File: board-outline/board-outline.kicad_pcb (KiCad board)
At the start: 2 copper layers, 162 x 136.8 mm, 1 part

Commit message: all done :)
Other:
- board size 162 x 136.8 mm -> 160 x 136.8 mm
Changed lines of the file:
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@@
 	)
 	(footprint "691378140024-2:J_Wurth_WR-TBL_691378140024"
+		(locked yes)
 		(layer "F.Cu")
 		(at 234.25 110.14 180)
@@
 			)
 		)
-		(attr through_hole)
+		(attr through_hole dnp)
 		(duplicate_pad_numbers_are_jumpers no)
 		(fp_line
@@
 		(layer "F.SilkS")
 	)
+	(gr_line
+		(start 190.39 80)
+		(end 194 80)
+		(stroke
+			(width 0.1)
+			(type default)
+		)
+		(locked yes)
+		(layer "F.SilkS")
+	)
+	(gr_line
+		(start 190.39 99.53)
+		(end 190.39 80)
+		(stroke
+			(width 0.1)
+			(type default)
+		)
+		(locked yes)
+		(layer "F.SilkS")
+	)
+	(gr_line
+		(start 239.61 80)
+		(end 236 80)
+		(stroke
+			(width 0.1)
+			(type default)
+		)
+		(locked yes)
+		(layer "F.SilkS")
+	)
+	(gr_line
+		(start 239.61 99.53)
+		(end 239.61 80)
+		(stroke
+			(width 0.1)
+			(type default)
+		)
+		(locked yes)
+		(layer "F.SilkS")
+	)
 	(gr_poly
 		(pts
@@
 	(gr_line
 		(start 135 93.5)
-		(end 135 165.5)
-		(stroke
-			(width 0.05)
-			(type default)
-		)
-		(layer "Edge.Cuts")
-	)
-	(gr_line
-		(start 155 93.5)
+		(end 155 93.5)
+		(stroke
+			(width 0.05)
+			(type solid)
+		)
+		(locked yes)
+		(layer "Edge.Cuts")
+	)
+	(gr_line
+		(start 135 165.5)
 		(end 135 93.5)
 		(stroke
 			(width 0.05)
-			(type default)
-		)
+			(type solid)
+		)
+		(locked yes)
 		(layer "Edge.Cuts")
 	)
@@
 		(stroke
 			(width 0.05)
-			(type default)
-		)
+			(type solid)
+		)
+		(locked yes)
 		(layer "Edge.Cuts")
 	)
@@
 		(stroke
 			(width 0.05)
-			(type default)
-		)
+			(type solid)
+		)
+		(locked yes)
 		(layer "Edge.Cuts")
 	)
@@
 			(type default)
 		)
+		(locked yes)
 		(layer "Edge.Cuts")
 	)
@@
 			(type default)
 		)
+		(locked yes)
 		(layer "Edge.Cuts")
 	)
@@
 		(stroke
 			(width 0.05)
-			(type default)
-		)
+			(type solid)
+		)
+		(locked yes)
 		(layer "Edge.Cuts")
 	)
@@
 			(type default)
 		)
+		(locked yes)
 		(layer "Edge.Cuts")
 	)
 	(gr_rect
 		(start 275 93.5)
-		(end 297 165.5)
-		(stroke
-			(width 0.05)
-			(type default)
+		(end 295 165.5)
+		(stroke
+			(width 0.05)
+			(type solid)
 		)
 		(fill no)
+		(locked yes)
 		(layer "Edge.Cuts")
 	)
@@
 			)
 		)
+	)
+	(zone
+		(locked yes)
+		(layer "F.SilkS")
+		(hatch edge 0.5)
+		(connect_pads
+			(clearance 0)
+		)
+		(min_thickness 0.25)
+		(keepout
+			(tracks not_allowed)
+			(vias not_allowed)
+			(pads not_allowed)
+			(copperpour allowed)
+			(footprints not_allowed)
+		)
+		(placement
+			(enabled no)
+			(sheetname "")
+		)
+		(fill
+			(thermal_gap 0.5)
+			(thermal_bridge_width 0.5)
+			(island_removal_mode 0)
+		)
+		(polygon
+			(pts
+				(xy 239.61 99.53) (xy 239.61 80) (xy 190.4 80) (xy 190.4 99.121053)
+			)
+		)

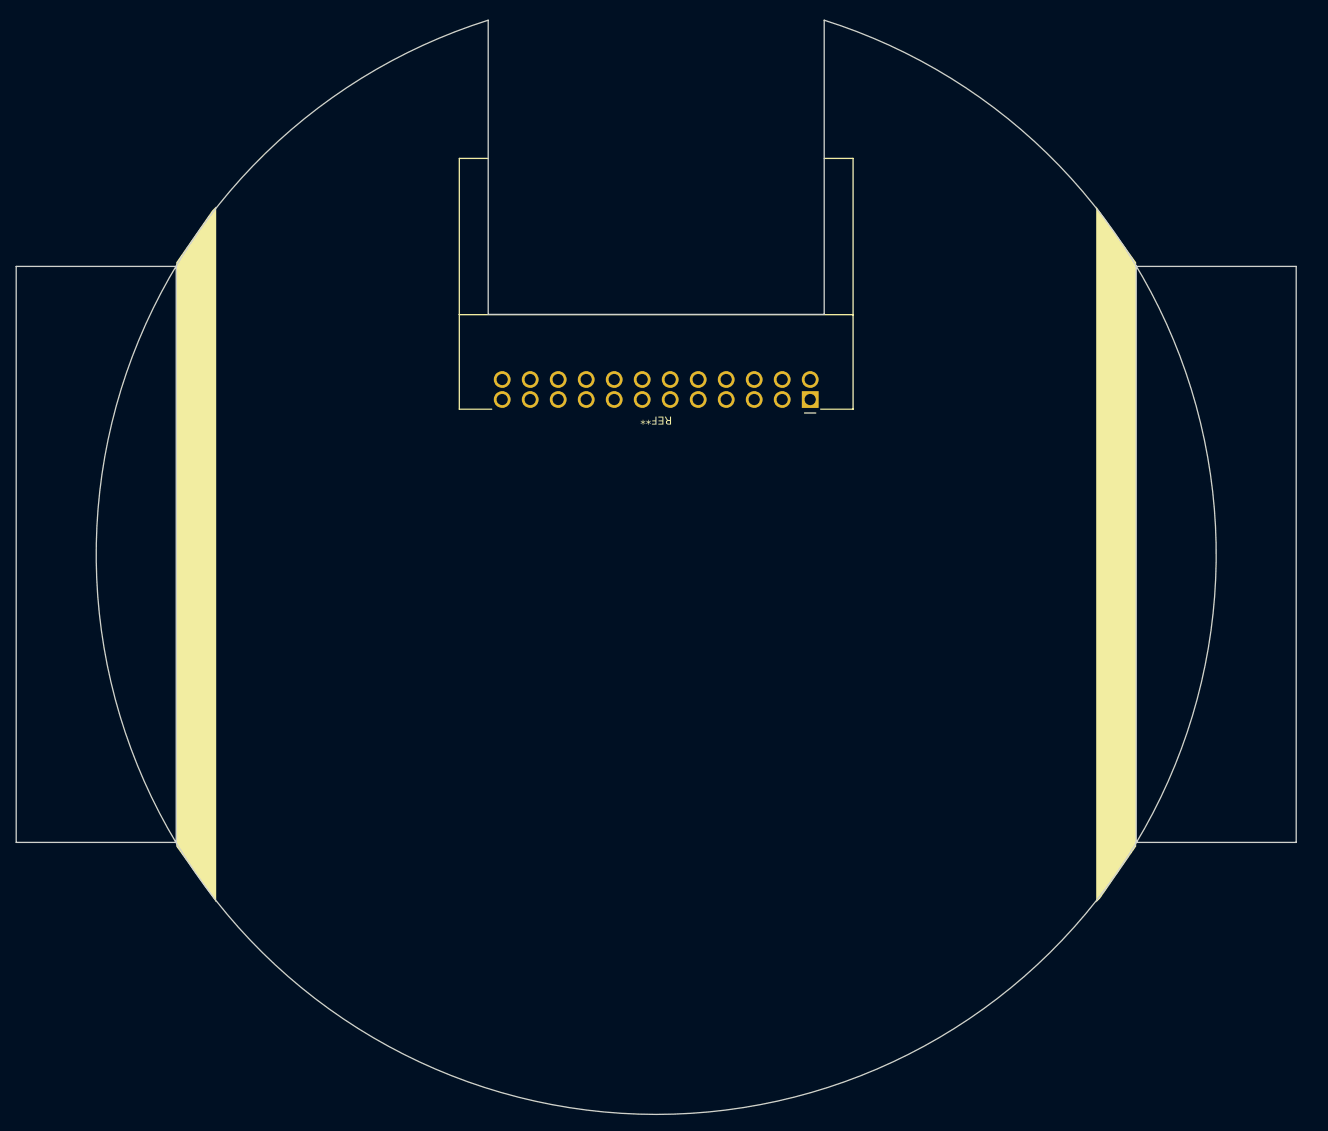
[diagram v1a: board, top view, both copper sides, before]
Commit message: finished board-outline fixed issues
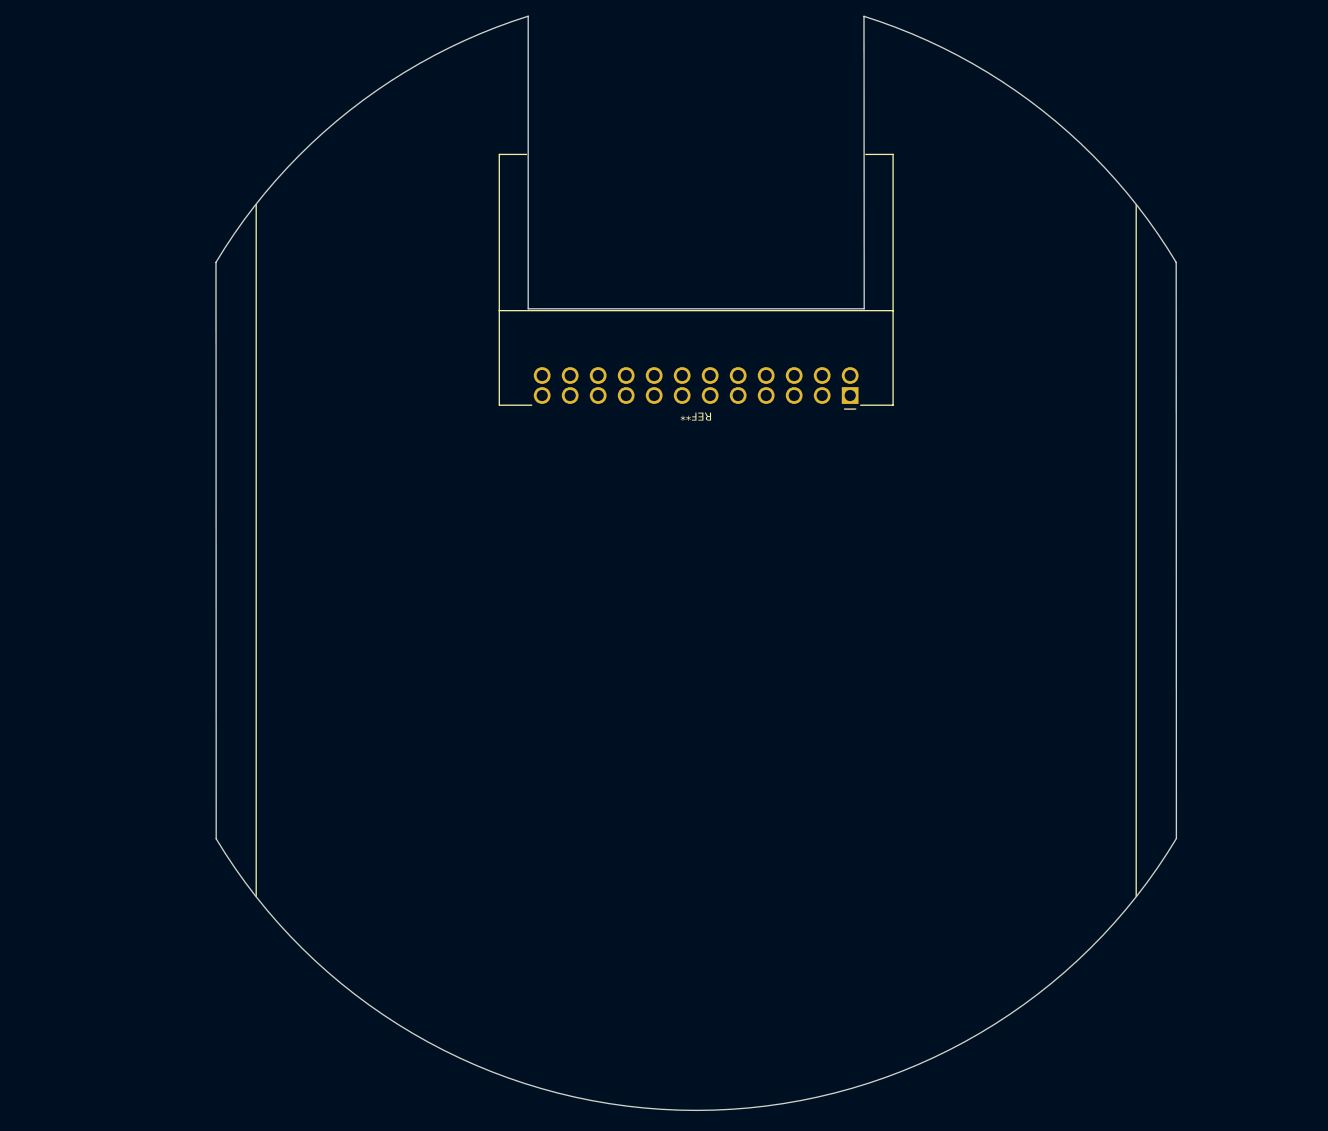
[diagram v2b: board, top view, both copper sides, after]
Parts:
- moved REF** 5.02 mm to (239.2, 109.6)
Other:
- board size 160 x 136.8 mm -> 120 x 136.8 mm
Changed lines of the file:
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@@
 		(capping no)
 		(filling no)
-		(grid_origin 250 200)
+		(grid_origin 220 129)
 		(pcbplotparams
 			(layerselection 0x00000000_00000000_55555555_575555f0)
@@
 		(locked yes)
 		(layer "F.Cu")
-		(at 234.25 110.14 180)
+		(at 239.25 109.64 180)
 		(descr "Series 3781 - PCB Header Dual Row - 3.5mm pitch - THT, body 49x11.6x10.8mm, https://www.we-online.com/en/components/products/datasheet/691378140024?ki")
 		(tags "THT Horizontal")
@@
 		)
 		(embedded_fonts no)
-		(model "${WE_3DMODEL_DIR}/Connector_THT_Wurth.3dshapes/J_Wurth_WR-TBL_691378140024.step"
+		(model "C:/Users/yamns/Documents/KiCad/10.0/3dmodels/STP_WR-TBL3_Series 3781 - PCB Header - 6913781400xx_691378140024 (rev1).stp"
 			(hide yes)
 			(offset
@@
 		)
 	)
-	(gr_poly
-		(pts
-			(xy 160 173) (xy 155 166) (xy 155 93) (xy 159.5 86.5) (xy 160 86)
-		)
-		(stroke
-			(width 0)
+	(gr_line
+		(start 165 172.25)
+		(end 165 85.75)
+		(stroke
+			(width 0.1)
+			(type default)
+		)
+		(layer "F.SilkS")
+	)
+	(gr_line
+		(start 195.39 79.5)
+		(end 198.8 79.5)
+		(stroke
+			(width 0.1)
+			(type default)
+		)
+		(locked yes)
+		(layer "F.SilkS")
+	)
+	(gr_line
+		(start 195.39 99.03)
+		(end 195.39 79.5)
+		(stroke
+			(width 0.1)
+			(type default)
+		)
+		(locked yes)
+		(layer "F.SilkS")
+	)
+	(gr_line
+		(start 244.61 79.5)
+		(end 241.2 79.5)
+		(stroke
+			(width 0.1)
+			(type default)
+		)
+		(locked yes)
+		(layer "F.SilkS")
+	)
+	(gr_line
+		(start 244.61 99.03)
+		(end 244.61 79.5)
+		(stroke
+			(width 0.1)
+			(type default)
+		)
+		(locked yes)
+		(layer "F.SilkS")
+	)
+	(gr_line
+		(start 275 85.75)
+		(end 275 172.25)
+		(stroke
+			(width 0.1)
+			(type default)
+		)
+		(layer "F.SilkS")
+	)
+	(gr_circle
+		(center 220 129)
+		(end 290 129)
+		(stroke
+			(width 0.1)
 			(type solid)
 		)
-		(fill yes)
-		(layer "F.SilkS")
-	)
-	(gr_poly
-		(pts
-			(xy 270 86) (xy 275 93) (xy 275 166) (xy 270.5 172.5) (xy 270 173)
-		)
-		(stroke
-			(width 0)
-			(type solid)
-		)
-		(fill yes)
-		(layer "F.SilkS")
-	)
-	(gr_line
-		(start 190.39 80)
-		(end 194 80)
-		(stroke
-			(width 0.1)
-			(type default)
-		)
-		(locked yes)
-		(layer "F.SilkS")
-	)
-	(gr_line
-		(start 190.39 99.53)
-		(end 190.39 80)
-		(stroke
-			(width 0.1)
-			(type default)
-		)
-		(locked yes)
-		(layer "F.SilkS")
-	)
-	(gr_line
-		(start 239.61 80)
-		(end 236 80)
-		(stroke
-			(width 0.1)
-			(type default)
-		)
-		(locked yes)
-		(layer "F.SilkS")
-	)
-	(gr_line
-		(start 239.61 99.53)
-		(end 239.61 80)
-		(stroke
-			(width 0.1)
-			(type default)
-		)
-		(locked yes)
-		(layer "F.SilkS")
-	)
-	(gr_poly
-		(pts
-			(xy 160 173) (xy 155 166) (xy 155 93) (xy 159.5 86.5) (xy 160 86)
-		)
-		(stroke
-			(width 0)
-			(type solid)
-		)
-		(fill yes)
-		(layer "B.SilkS")
-	)
-	(gr_poly
-		(pts
-			(xy 270 86) (xy 275 93) (xy 275 166) (xy 270.5 172.5) (xy 270 173)
-		)
-		(stroke
-			(width 0)
-			(type solid)
-		)
-		(fill yes)
-		(layer "B.SilkS")
-	)
-	(gr_line
-		(start 135 93.5)
-		(end 155 93.5)
-		(stroke
-			(width 0.05)
-			(type solid)
-		)
-		(locked yes)
-		(layer "Edge.Cuts")
-	)
-	(gr_line
-		(start 135 165.5)
-		(end 135 93.5)
-		(stroke
-			(width 0.05)
-			(type solid)
-		)
-		(locked yes)
-		(layer "Edge.Cuts")
-	)
-	(gr_line
-		(start 155 93.5)
-		(end 155 165.5)
-		(stroke
-			(width 0.05)
-			(type solid)
-		)
-		(locked yes)
-		(layer "Edge.Cuts")
-	)
-	(gr_line
-		(start 155 165.5)
-		(end 135 165.5)
-		(stroke
-			(width 0.05)
-			(type solid)
-		)
-		(locked yes)
-		(layer "Edge.Cuts")
-	)
-	(gr_line
-		(start 194 62.724256)
-		(end 194 99.5)
-		(stroke
-			(width 0.05)
-			(type default)
-		)
-		(locked yes)
-		(layer "Edge.Cuts")
-	)
-	(gr_line
-		(start 194 99.5)
-		(end 236 99.5)
+		(fill no)
+		(locked yes)
+		(layer "Cmts.User")
+	)
+	(gr_line
+		(start 159.975495 92.985297)
+		(end 160 165.055512)
 		(stroke
 			(width 0.05)
@@
 	)
 	(gr_arc
-		(start 236 62.724256)
-		(mid 215 199.5)
-		(end 194 62.724256)
-		(stroke
-			(width 0.05)
-			(type solid)
-		)
-		(locked yes)
-		(layer "Edge.Cuts")
-	)
-	(gr_line
-		(start 236 99.5)
-		(end 236 62.724256)
-		(stroke
-			(width 0.05)
-			(type default)
-		)
-		(locked yes)
-		(layer "Edge.Cuts")
-	)
-	(gr_rect
-		(start 275 93.5)
-		(end 295 165.5)
-		(stroke
-			(width 0.05)
-			(type solid)
-		)
-		(fill no)
+		(start 159.975495 92.985297)
+		(mid 176.666375 74.025488)
+		(end 199 62.224256)
+		(stroke
+			(width 0.05)
+			(type default)
+		)
+		(locked yes)
+		(layer "Edge.Cuts")
+	)
+	(gr_line
+		(start 199 62.224256)
+		(end 199 98.8)
+		(stroke
+			(width 0.05)
+			(type default)
+		)
+		(locked yes)
+		(layer "Edge.Cuts")
+	)
+	(gr_line
+		(start 199 98.8)
+		(end 241 98.8)
+		(stroke
+			(width 0.05)
+			(type default)
+		)
+		(locked yes)
+		(layer "Edge.Cuts")
+	)
+	(gr_arc
+		(start 240.975495 62.238959)
+		(mid 263.309119 74.040191)
+		(end 280 93)
+		(stroke
+			(width 0.05)
+			(type default)
+		)
+		(locked yes)
+		(layer "Edge.Cuts")
+	)
+	(gr_line
+		(start 241 98.8)
+		(end 240.975495 62.238959)
+		(stroke
+			(width 0.05)
+			(type default)
+		)
+		(locked yes)
+		(layer "Edge.Cuts")
+	)
+	(gr_arc
+		(start 280.024504 165.014702)
+		(mid 220.0238 198.999995)
+		(end 160 165.05551)
+		(stroke
+			(width 0.05)
+			(type default)
+		)
+		(locked yes)
+		(layer "Edge.Cuts")
+	)
+	(gr_line
+		(start 280.024504 165.014702)
+		(end 280 93)
+		(stroke
+			(width 0.05)
+			(type default)
+		)
 		(locked yes)
 		(layer "Edge.Cuts")
 	)
 	(zone
-		(layers "F.Cu" "B.Cu")
-		(name "no-place right")
+		(locked yes)
+		(layer "F.Cu")
 		(hatch edge 0.5)
 		(connect_pads
@@
 		(polygon
 			(pts
-				(xy 160 173) (xy 160 86) (xy 159.5 86.5) (xy 157 90) (xy 155 93) (xy 155 166) (xy 157 169)
+				(xy 280 165) (xy 280 93) (xy 275 85.8) (xy 275 172.2)
 			)
 		)
 	)
 	(zone
-		(layers "F.Cu" "B.Cu")
-		(name "no-place right")
+		(locked yes)
+		(layer "F.Cu")
 		(hatch edge 0.5)
 		(connect_pads
@@
 		(polygon
 			(pts
-				(xy 270 86) (xy 270 173) (xy 270.5 172.5) (xy 273 169) (xy 275 166) (xy 275 93) (xy 273 90)
+				(xy 160 165) (xy 165 172.25) (xy 165 85.75) (xy 160 93)
 			)
 		)
@@
 		(polygon
 			(pts
-				(xy 239.61 99.53) (xy 239.61 80) (xy 190.4 80) (xy 190.4 99.121053)
-			)
-		)
+				(xy 244.61 99.03) (xy 244.61 79.5) (xy 195.4 79.5) (xy 195.4 98.621053)
+			)
+		)

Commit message: New standard board
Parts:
- moved REF** 1.00 mm to (239.2, 108.6)
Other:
- board size 120 x 136.8 mm -> 120 x 132 mm

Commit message: Fixa board outkube
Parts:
- moved REF** 6.75 mm to (239.2, 115.4)
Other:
- board size 120 x 132 mm -> 110 x 122.5 mm

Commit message: Fiksa standard board outline
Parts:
- added REF**: Standardkonnektor_plugg, TestPoint:TestPoint_Pad_1.0x1.0mm, F.Cu at (220.0, 99.0)
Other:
- outline, holes or cut-outs redrawn
